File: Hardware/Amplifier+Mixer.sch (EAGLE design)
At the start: 192 parts, among them IC1 7812, IC2 7805, IC3 7912, IC4 OPA134PA, IC5 OPA134PA, IC6 MEGA8-AI, IC8 LM358D, IC9 LM358D, J1 6MM, J10 JST-XH2, J2 6MM, J3 6MM, J4 6MM, J5 TERMINAL-BLOCK-2PLUG-IN, J6 TERMINAL-BLOCK-2PLUG-IN, J7 ENCODER, J8 DISPLAY, J9 USB, K1 12V 8A, K2 12V 8A, T1 BC817, T2 BC817, T3 BC817, U1 LM1117-3.3, U2 10k, U3 10k, U4 10k, U5 10k, U6 TDA7498L, U7 10k, U8 10k, U9 MCP9700SMD, X1 RCA-4-CHANNEL, X2 JST-XH2, X3 ICSP, X4 JST-XH2

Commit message: added indicator LED to audio detection circuit
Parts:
- added LED1: (no value), led:LEDCHIP-LED0603
- added R43: 1k, rcl:R-EU_R0603
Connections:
- new net N$37: LED1.A, R43.2
- net +3V3: now also U2G1.!WP, U3G1.!WP, U4G1.!WP, U5G1.!WP, U7G1.!WP, U8G1.!WP
- net DGND: now also LED1.C
- net N$36: now also R43.1
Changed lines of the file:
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@@
 <part name="P+11" library="supply1" library_urn="urn:adsk.eagle:library:371" deviceset="+5V" device=""/>
 <part name="SUPPLY28" library="supply2" library_urn="urn:adsk.eagle:library:372" deviceset="DGND" device=""/>
+<part name="+3V4" library="supply1" library_urn="urn:adsk.eagle:library:371" deviceset="+3V3" device=""/>
+<part name="LED1" library="led" library_urn="urn:adsk.eagle:library:259" deviceset="LED" device="CHIP-LED0603" package3d_urn="urn:adsk.eagle:package:15819/3"/>
+<part name="R43" library="rcl" library_urn="urn:adsk.eagle:library:334" deviceset="R-EU_" device="R0603" package3d_urn="urn:adsk.eagle:package:23555/3" value="1k">
+<spice>
+<pinmapping spiceprefix="R">
+<pinmap gate="G$1" pin="1" pinorder="1"/>
+<pinmap gate="G$1" pin="2" pinorder="2"/>
+</pinmapping>
+</spice>
+<attribute name="CONRAD" value="1585255 - 62"/>
+<attribute name="MOUSER" value="603-RC0603FR-071KL"/>
+<attribute name="STOCK" value="3"/>
+</part>
+<part name="SUPPLY42" library="supply2" library_urn="urn:adsk.eagle:library:372" deviceset="DGND" device=""/>
 </parts>
 <sheets>
@@
 <attribute name="VALUE" x="175.26" y="56.896" size="1.778" layer="96" align="top-center"/>
 </instance>
+<instance part="+3V4" gate="G$1" x="256.54" y="25.4" smashed="yes">
+<attribute name="VALUE" x="256.54" y="25.654" size="1.778" layer="96" align="bottom-center"/>
+</instance>
+<instance part="LED1" gate="G$1" x="614.68" y="167.64" smashed="yes">
+<attribute name="NAME" x="618.236" y="163.068" size="1.778" layer="95" rot="R90"/>
+<attribute name="VALUE" x="620.395" y="163.068" size="1.778" layer="96" rot="R90"/>
+</instance>
+<instance part="R43" gate="G$1" x="614.68" y="175.26" smashed="yes" rot="R270">
+<attribute name="NAME" x="613.537" y="180.34" size="1.778" layer="95" rot="R90" align="bottom-center"/>
+<attribute name="VALUE" x="615.823" y="175.26" size="1.778" layer="96" rot="R90" align="top-center"/>
+<attribute name="CONRAD" x="614.68" y="175.26" size="1.778" layer="96" rot="R90" display="off"/>
+<attribute name="MOUSER" x="614.68" y="175.26" size="1.778" layer="96" rot="R90" display="off"/>
+<attribute name="STOCK" x="614.68" y="175.26" size="1.778" layer="96" rot="R90" display="off"/>
+</instance>
+<instance part="SUPPLY42" gate="G$1" x="614.68" y="160.02" smashed="yes">
+<attribute name="VALUE" x="614.68" y="158.496" size="1.778" layer="96" align="top-center"/>
+</instance>
 </instances>
 <busses>
@@
 <pinref part="+3V315" gate="G$1" pin="+3V3"/>
 <wire x1="256.54" y1="43.18" x2="256.54" y2="45.72" width="0.1524" layer="91"/>
+<pinref part="U7" gate="G1" pin="!WP"/>
+<wire x1="251.46" y1="45.72" x2="256.54" y2="45.72" width="0.1524" layer="91"/>
+<junction x="256.54" y="45.72"/>
 </segment>
 <segment>
@@
 <wire x1="256.54" y1="63.5" x2="256.54" y2="68.58" width="0.1524" layer="91"/>
 <pinref part="+3V313" gate="G$1" pin="+3V3"/>
+<pinref part="U5" gate="G1" pin="!WP"/>
+<wire x1="251.46" y1="68.58" x2="256.54" y2="68.58" width="0.1524" layer="91"/>
+<junction x="256.54" y="68.58"/>
 </segment>
 <segment>
@@
 <wire x1="256.54" y1="86.36" x2="256.54" y2="88.9" width="0.1524" layer="91"/>
 <junction x="256.54" y="88.9"/>
+<pinref part="U4" gate="G1" pin="!WP"/>
+<wire x1="251.46" y1="91.44" x2="256.54" y2="91.44" width="0.1524" layer="91"/>
+<junction x="256.54" y="91.44"/>
 </segment>
 <segment>
@@
 <wire x1="251.46" y1="106.68" x2="256.54" y2="106.68" width="0.1524" layer="91"/>
 <wire x1="256.54" y1="106.68" x2="256.54" y2="114.3" width="0.1524" layer="91"/>
+<pinref part="U3" gate="G1" pin="!WP"/>
+<wire x1="251.46" y1="114.3" x2="256.54" y2="114.3" width="0.1524" layer="91"/>
+<junction x="256.54" y="114.3"/>
 </segment>
 <segment>
@@
 <wire x1="256.54" y1="129.54" x2="256.54" y2="134.62" width="0.1524" layer="91"/>
 <junction x="256.54" y="134.62"/>
+<pinref part="U2" gate="G1" pin="!WP"/>
+<wire x1="251.46" y1="137.16" x2="256.54" y2="137.16" width="0.1524" layer="91"/>
+<junction x="256.54" y="137.16"/>
 </segment>
 <segment>
@@
 <wire x1="464.82" y1="187.96" x2="464.82" y2="195.58" width="0.1524" layer="91"/>
 </segment>
+<segment>
+<pinref part="U8" gate="G1" pin="!WP"/>
+<pinref part="+3V4" gate="G$1" pin="+3V3"/>
+<wire x1="251.46" y1="22.86" x2="256.54" y2="22.86" width="0.1524" layer="91"/>
+</segment>
 </net>
 <net name="AUDIO_DETECT" class="0">
@@
 <pinref part="IC9" gate="B" pin="OUT"/>
 <wire x1="612.14" y1="187.96" x2="614.68" y2="187.96" width="0.1524" layer="91"/>
+<pinref part="R43" gate="G$1" pin="1"/>
+<wire x1="614.68" y1="180.34" x2="614.68" y2="187.96" width="0.1524" layer="91"/>
+<junction x="614.68" y="187.96"/>
 </segment>
 </net>
@@
 <junction x="175.26" y="60.96"/>
 </segment>
+<segment>
+<pinref part="LED1" gate="G$1" pin="C"/>
+<pinref part="SUPPLY42" gate="G$1" pin="DGND"/>
+</segment>
 </net>
 <net name="AGND" class="0">
@@
 </segment>
 </net>
+<net name="N$37" class="0">
+<segment>
+<pinref part="R43" gate="G$1" pin="2"/>
+<pinref part="LED1" gate="G$1" pin="A"/>
+</segment>
+</net>

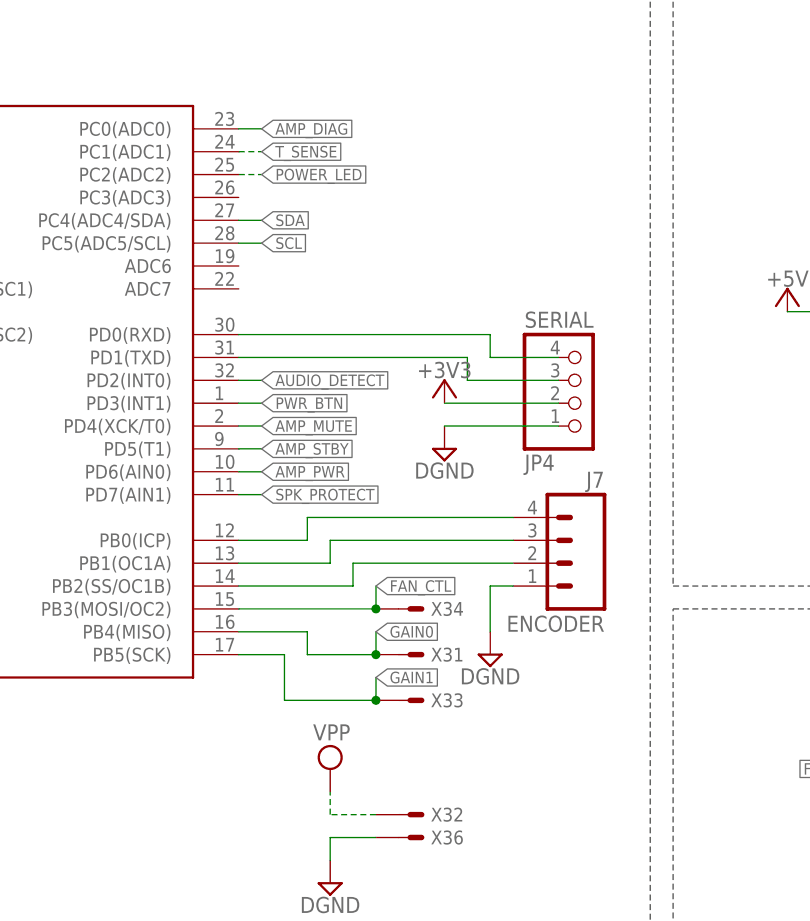
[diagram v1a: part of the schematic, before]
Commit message: moved power led to pwm capable pin
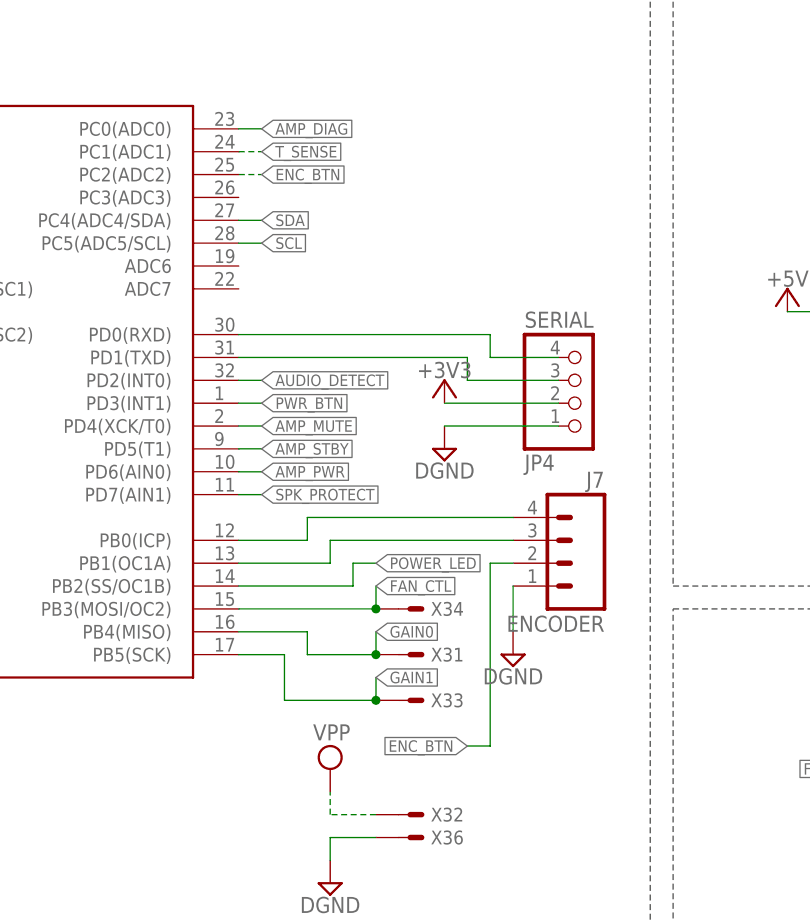
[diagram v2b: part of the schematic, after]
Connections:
- removed net N$45: IC6.PB2(SS/OC1B), J7.2
- new net ENC_BTN: IC6.PC2(ADC2), J7.2
- net POWER_LED: now also IC6.PB2(SS/OC1B); no longer IC6.PC2(ADC2)
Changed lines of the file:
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@@
 <attribute name="STOCK" x="116.84" y="53.34" size="1.778" layer="96" display="off"/>
 </instance>
-<instance part="SUPPLY18" gate="G$1" x="109.22" y="43.18" smashed="yes">
-<attribute name="VALUE" x="109.22" y="41.656" size="1.778" layer="96" align="top-center"/>
+<instance part="SUPPLY18" gate="G$1" x="111.76" y="43.18" smashed="yes">
+<attribute name="VALUE" x="111.76" y="41.656" size="1.778" layer="96" align="top-center"/>
 </instance>
 <instance part="KK2" gate="G$1" x="233.68" y="200.66" smashed="yes">
@@
 <pinref part="J7" gate="G$1" pin="1"/>
 <pinref part="SUPPLY18" gate="G$1" pin="DGND"/>
-<wire x1="111.76" y1="50.8" x2="109.22" y2="50.8" width="0.1524" layer="91"/>
-<wire x1="109.22" y1="50.8" x2="109.22" y2="45.72" width="0.1524" layer="91"/>
+<wire x1="111.76" y1="50.8" x2="111.76" y2="45.72" width="0.1524" layer="91"/>
 </segment>
 <segment>
@@
 </segment>
 </net>
-<net name="N$45" class="0">
-<segment>
-<pinref part="J7" gate="G$1" pin="2"/>
-<wire x1="111.76" y1="53.34" x2="93.98" y2="53.34" width="0.1524" layer="91"/>
-<wire x1="93.98" y1="53.34" x2="93.98" y2="50.8" width="0.1524" layer="91"/>
-<pinref part="IC6" gate="G$1" pin="PB2(SS/OC1B)"/>
-<wire x1="93.98" y1="50.8" x2="81.28" y2="50.8" width="0.1524" layer="91"/>
-</segment>
-</net>
 <net name="N$76" class="0">
 <segment>
@@
 </segment>
 <segment>
+<pinref part="IC6" gate="G$1" pin="PB2(SS/OC1B)"/>
+<wire x1="93.98" y1="50.8" x2="81.28" y2="50.8" width="0.1524" layer="91"/>
+<label x="96.52" y="53.34" size="1.27" layer="95" xref="yes"/>
+<wire x1="93.98" y1="50.8" x2="93.98" y2="53.34" width="0.1524" layer="91"/>
+<wire x1="93.98" y1="53.34" x2="96.52" y2="53.34" width="0.1524" layer="91"/>
+</segment>
+</net>
+<net name="N$37" class="0">
+<segment>
+<pinref part="R43" gate="G$1" pin="2"/>
+<pinref part="LED1" gate="G$1" pin="A"/>
+</segment>
+</net>
+<net name="ENC_BTN" class="0">
+<segment>
+<pinref part="J7" gate="G$1" pin="2"/>
+<wire x1="111.76" y1="53.34" x2="109.22" y2="53.34" width="0.1524" layer="91"/>
+<wire x1="109.22" y1="53.34" x2="109.22" y2="33.02" width="0.1524" layer="91"/>
+<wire x1="109.22" y1="33.02" x2="106.68" y2="33.02" width="0.1524" layer="91"/>
+<label x="106.68" y="33.02" size="1.27" layer="95" rot="R180" xref="yes"/>
+</segment>
+<segment>
 <pinref part="IC6" gate="G$1" pin="PC2(ADC2)"/>
 <wire x1="81.28" y1="96.52" x2="83.82" y2="96.52" width="0.1524" layer="91" style="longdash"/>
@@
 </segment>
 </net>
-<net name="N$37" class="0">
-<segment>
-<pinref part="R43" gate="G$1" pin="2"/>
-<pinref part="LED1" gate="G$1" pin="A"/>
-</segment>
-</net>

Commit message: fixed feedback network in mixer buffer output stage
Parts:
- IC4, IC5: value OPA134PA -> LME49720NA; CONRAD 1011117 - 62 -> 1010937 - 62; MOUSER 595-OPA134PA -> (none)
- U9: value MCP9700SMD -> MCP9701SMD
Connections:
- removed net N$52: IC4A.-IN, R18.1
- new net N$45: IC4A.-IN, R18.1, R21.2
- net AGND: no longer R21.2, R42.2
- net N$44: now also R42.2
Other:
- moved on the sheet: C17, C18, C19, C20, C21, C22, C24, C25, C26, C27, C30, C31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

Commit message: updated to newest version
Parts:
- IC1: value 7812 -> LM2940CT-12; CONRAD 179230 - 62 -> 1013996 - 62
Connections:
- new net VDD: C62.2, R27.2, U6.VDDS
- net +3V3: no longer C62.2, R27.2, U6.VDDS
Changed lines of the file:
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@@
 <attribute name="STOCK" value="1"/>
 </part>
-<part name="IC1" library="v-reg" library_urn="urn:adsk.eagle:library:409" deviceset="78XXS" device="" package3d_urn="urn:adsk.eagle:package:30342/1" value="7812">
-<attribute name="CONRAD" value="179230 - 62"/>
+<part name="IC1" library="v-reg" library_urn="urn:adsk.eagle:library:409" deviceset="78XXS" device="" package3d_urn="urn:adsk.eagle:package:30342/1" value="LM2940CT-12">
+<attribute name="CONRAD" value="1013996 - 62"/>
 <attribute name="MOUSER" value="511-L7812CV"/>
 <attribute name="STOCK" value="1"/>
@@
 </part>
 <part name="PE2" library="supply1" library_urn="urn:adsk.eagle:library:371" deviceset="PE" device=""/>
-<part name="+3V312" library="supply1" library_urn="urn:adsk.eagle:library:371" deviceset="+3V3" device=""/>
 <part name="C49" library="rcl" library_urn="urn:adsk.eagle:library:334" deviceset="C-EU" device="C0603" package3d_urn="urn:adsk.eagle:package:23616/2" value="100n">
 <spice>
@@
 <attribute name="STOCK" value="24"/>
 </part>
-<part name="+3V319" library="supply1" library_urn="urn:adsk.eagle:library:371" deviceset="+3V3" device=""/>
 <part name="AGND20" library="supply1" library_urn="urn:adsk.eagle:library:371" deviceset="AGND" device=""/>
 <part name="C60" library="rcl" library_urn="urn:adsk.eagle:library:334" deviceset="CPOL-EU" device="153CLV-0505" package3d_urn="urn:adsk.eagle:package:23402/2" value="10µ 10V">
@@
 </part>
 <part name="SUPPLY42" library="supply2" library_urn="urn:adsk.eagle:library:372" deviceset="DGND" device=""/>
+<part name="VDD1" library="supply1" library_urn="urn:adsk.eagle:library:371" deviceset="VDD" device=""/>
+<part name="VDD2" library="supply1" library_urn="urn:adsk.eagle:library:371" deviceset="VDD" device=""/>
 </parts>
 <sheets>
@@
 <attribute name="VALUE" x="586.74" y="0.762" size="1.778" layer="96" align="top-center"/>
 </instance>
-<instance part="+3V312" gate="G$1" x="518.16" y="71.12" smashed="yes">
-<attribute name="VALUE" x="518.16" y="71.374" size="1.778" layer="96" align="bottom-center"/>
-</instance>
 <instance part="C49" gate="G$1" x="541.02" y="53.34" smashed="yes">
 <attribute name="NAME" x="538.988" y="50.5968" size="1.778" layer="95" rot="R180" align="top-left"/>
@@
 <attribute name="STOCK" x="538.48" y="10.16" size="1.778" layer="96" display="off"/>
 </instance>
-<instance part="+3V319" gate="G$1" x="508" y="15.24" smashed="yes">
-<attribute name="VALUE" x="508" y="15.494" size="1.778" layer="96" align="bottom-center"/>
-</instance>
 <instance part="AGND20" gate="VR1" x="596.9" y="2.54" smashed="yes">
 <attribute name="VALUE" x="596.9" y="1.778" size="1.778" layer="96" align="top-center"/>
@@
 <attribute name="VALUE" x="614.68" y="158.496" size="1.778" layer="96" align="top-center"/>
 </instance>
+<instance part="VDD1" gate="G$1" x="518.16" y="71.12" smashed="yes">
+<attribute name="VALUE" x="515.62" y="68.58" size="1.778" layer="96" rot="R90"/>
+</instance>
+<instance part="VDD2" gate="G$1" x="508" y="15.24" smashed="yes">
+<attribute name="VALUE" x="505.46" y="12.7" size="1.778" layer="96" rot="R90"/>
+</instance>
 </instances>
 <busses>
@@
 </segment>
 <segment>
-<pinref part="R27" gate="G$1" pin="2"/>
-<pinref part="+3V312" gate="G$1" pin="+3V3"/>
-<wire x1="518.16" y1="68.58" x2="518.16" y2="66.04" width="0.1524" layer="91"/>
-<pinref part="U6" gate="G$1" pin="VDDS"/>
-<wire x1="548.64" y1="63.5" x2="548.64" y2="60.96" width="0.1524" layer="91"/>
-<wire x1="548.64" y1="60.96" x2="523.24" y2="60.96" width="0.1524" layer="91"/>
-<wire x1="523.24" y1="60.96" x2="523.24" y2="66.04" width="0.1524" layer="91"/>
-<wire x1="523.24" y1="66.04" x2="518.16" y2="66.04" width="0.1524" layer="91" style="longdash"/>
-<junction x="518.16" y="66.04"/>
-</segment>
-<segment>
-<pinref part="C62" gate="G$1" pin="2"/>
-<wire x1="533.4" y1="10.16" x2="508" y2="10.16" width="0.1524" layer="91"/>
-<wire x1="508" y1="10.16" x2="508" y2="12.7" width="0.1524" layer="91"/>
-<pinref part="+3V319" gate="G$1" pin="+3V3"/>
-</segment>
-<segment>
 <pinref part="U7" gate="G1" pin="A0/HVP"/>
 <wire x1="251.46" y1="43.18" x2="256.54" y2="43.18" width="0.1524" layer="91"/>
@@
 </segment>
 </net>
+<net name="VDD" class="0">
+<segment>
+<pinref part="R27" gate="G$1" pin="2"/>
+<wire x1="518.16" y1="68.58" x2="518.16" y2="66.04" width="0.1524" layer="91"/>
+<pinref part="U6" gate="G$1" pin="VDDS"/>
+<wire x1="548.64" y1="63.5" x2="548.64" y2="60.96" width="0.1524" layer="91"/>
+<wire x1="548.64" y1="60.96" x2="523.24" y2="60.96" width="0.1524" layer="91"/>
+<wire x1="523.24" y1="60.96" x2="523.24" y2="66.04" width="0.1524" layer="91"/>
+<wire x1="523.24" y1="66.04" x2="518.16" y2="66.04" width="0.1524" layer="91" style="longdash"/>
+<junction x="518.16" y="66.04"/>
+<pinref part="VDD1" gate="G$1" pin="VDD"/>
+</segment>
+<segment>
+<pinref part="C62" gate="G$1" pin="2"/>
+<wire x1="533.4" y1="10.16" x2="508" y2="10.16" width="0.1524" layer="91"/>
+<wire x1="508" y1="10.16" x2="508" y2="12.7" width="0.1524" layer="91"/>
+<pinref part="VDD2" gate="G$1" pin="VDD"/>
+</segment>
+</net>
